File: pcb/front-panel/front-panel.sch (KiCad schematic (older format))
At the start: 26 parts, among them J1 HEADER-1x05, J2 HEADER-1x01, J3 HEADER-1x01, J4 HEADER-1x01, J5 HEADER-1x01, U1 ER-OLED1602-4W, U2 LT1109CS8-12

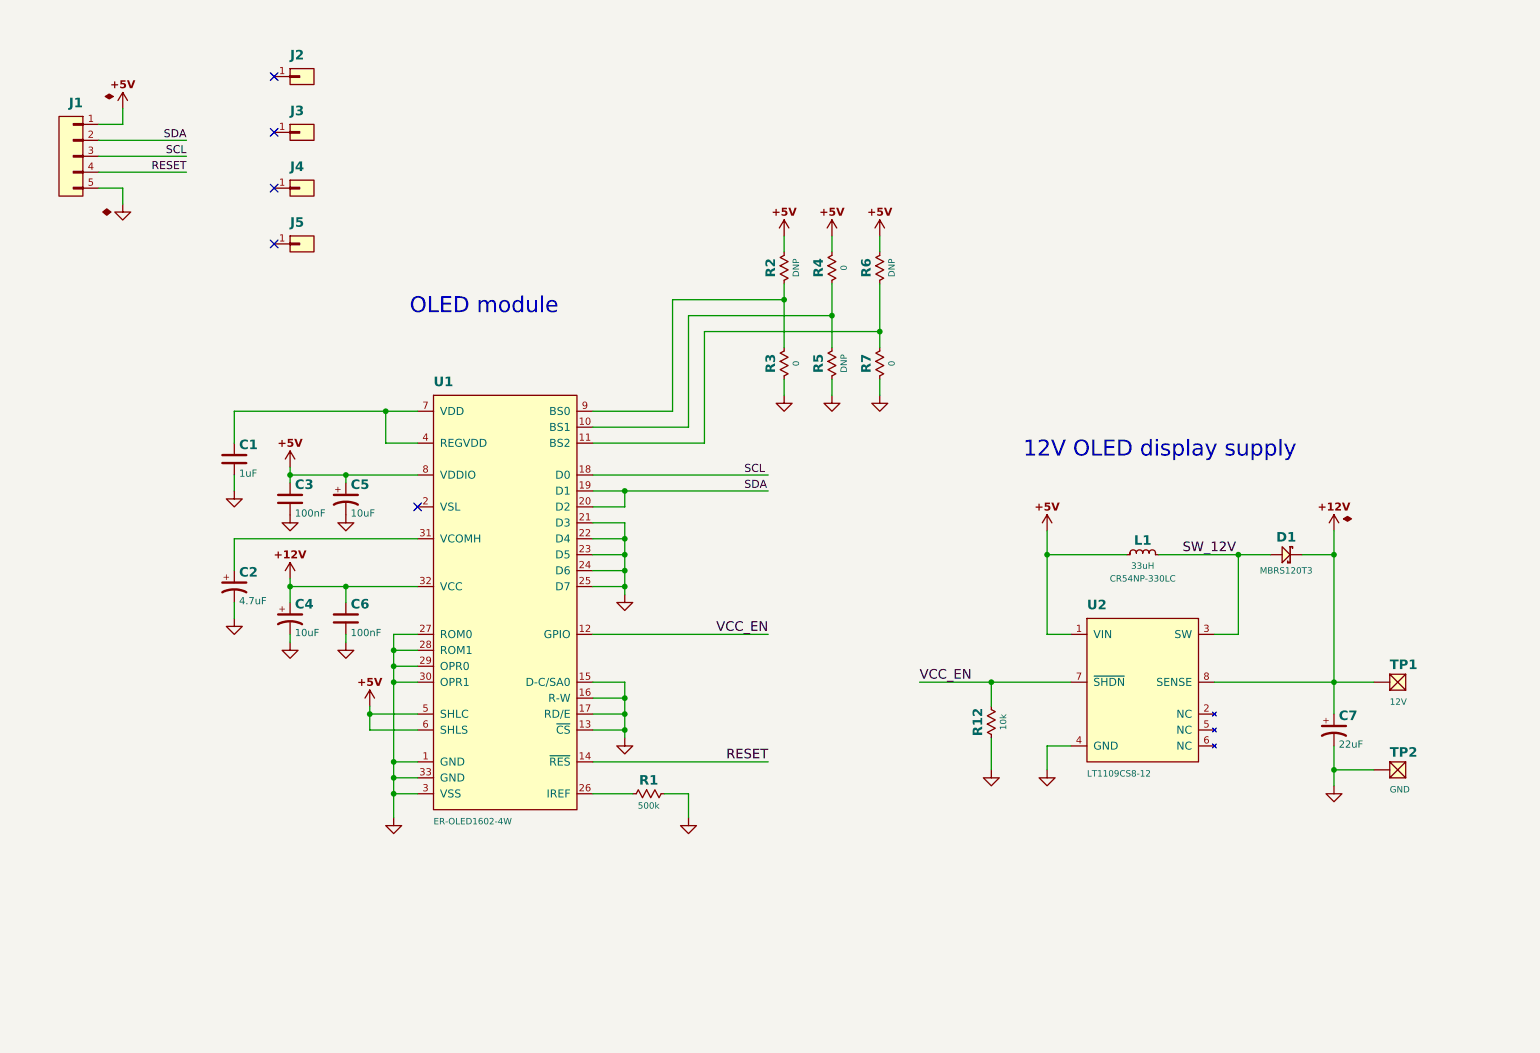
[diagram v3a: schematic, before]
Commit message: EN of 12V suply controlled from MCU instead of LCD GPIO
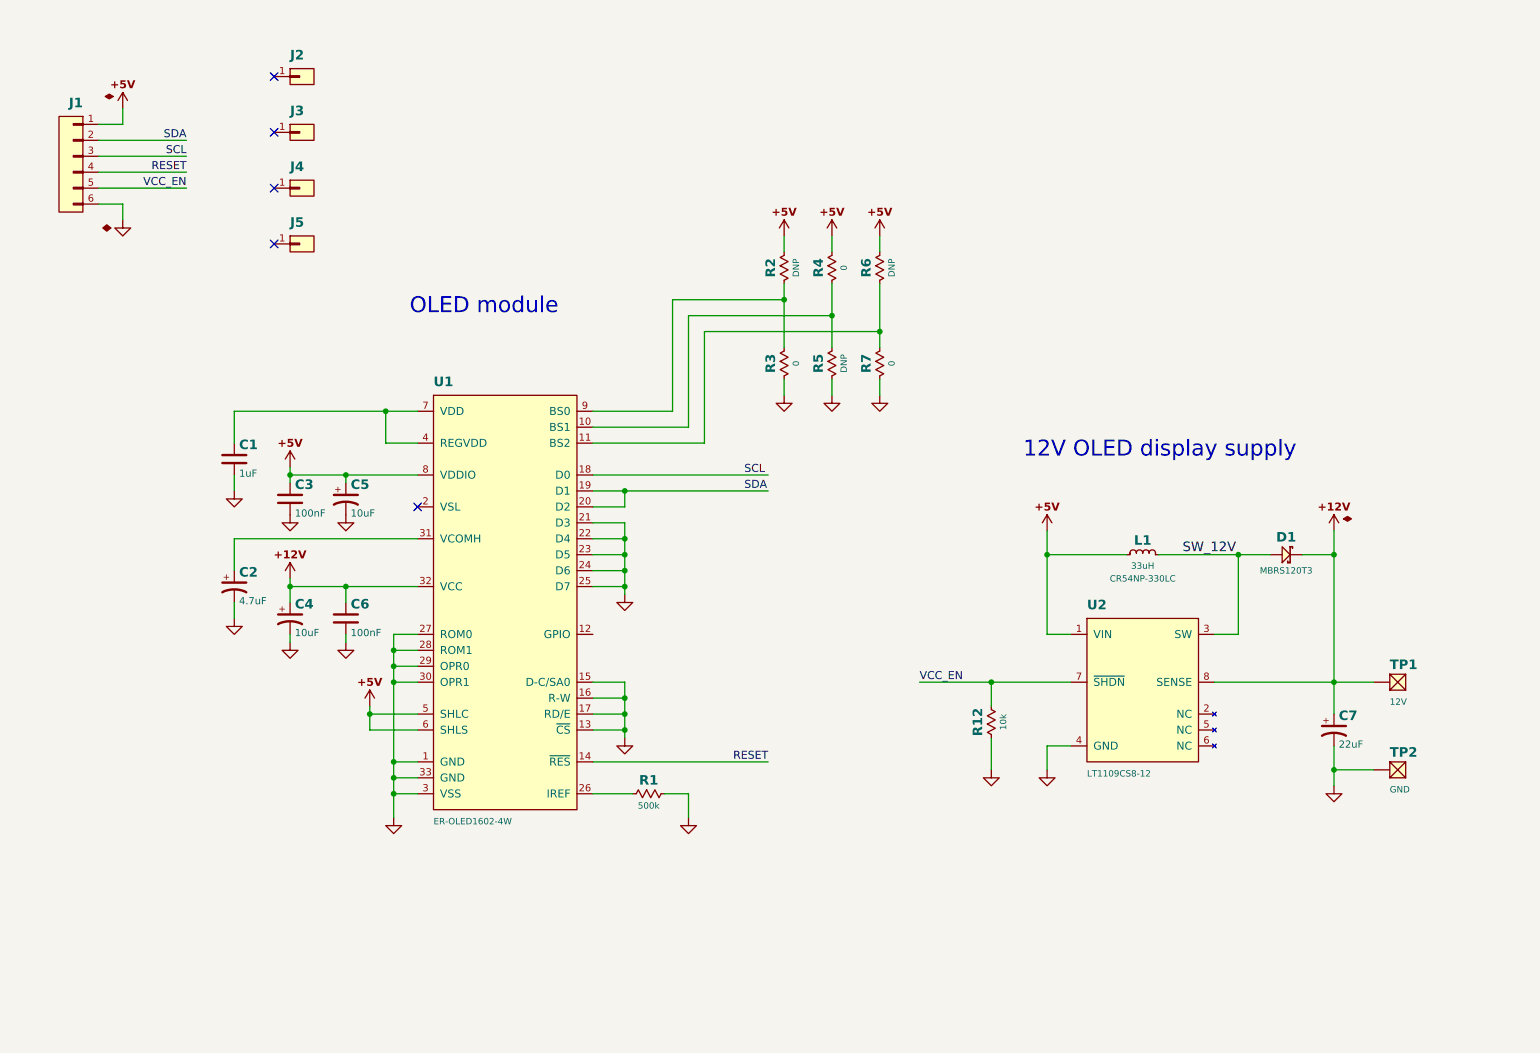
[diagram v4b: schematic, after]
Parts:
- removed J1: HEADER-1x05, Conn-Wire-Pads:WP-50mil-1x05, symbol HEADER-1x05
- added J1: HEADER-1x06, Conn-Wire-Pads:WP-50mil-1x06, symbol HEADER-1x06
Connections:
- net +5V: now also J1.1 (P1)
- net GND: now also J1.6 (P6)
- net RESET: now also J1.4 (P4)
- net SCL: now also J1.3 (P3)
- net SDA: now also J1.2 (P2)
- net VCC_EN: now also J1.5 (P5); no longer U1.12 (GPIO)
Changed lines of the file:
@@
 $EndComp
 $Comp
-L GND #PWR01
+L GND #PWR12
 U 1 1 562D385F
 P 3350 5800
-F 0 "#PWR01" H 3350 5850 30  0001 C CNN
+F 0 "#PWR12" H 3350 5850 30  0001 C CNN
 F 1 "GND" H 3350 5675 30  0001 C CNN
 F 2 "" H 3350 5800 60  0000 C CNN
@@
 $EndComp
 $Comp
-L GND #PWR02
+L GND #PWR15
 U 1 1 562D3A86
 P 5200 5800
-F 0 "#PWR02" H 5200 5850 30  0001 C CNN
+F 0 "#PWR15" H 5200 5850 30  0001 C CNN
 F 1 "GND" H 5200 5675 30  0001 C CNN
 F 2 "" H 5200 5800 60  0000 C CNN
@@
 $EndComp
 $Comp
-L GND #PWR03
+L GND #PWR13
 U 1 1 562D3B1B
 P 4800 4400
-F 0 "#PWR03" H 4800 4450 30  0001 C CNN
+F 0 "#PWR13" H 4800 4450 30  0001 C CNN
 F 1 "GND" H 4800 4275 30  0001 C CNN
 F 2 "" H 4800 4400 60  0000 C CNN
@@
 $EndComp
 $Comp
-L GND #PWR04
+L GND #PWR14
 U 1 1 562D3DB7
 P 4800 5300
-F 0 "#PWR04" H 4800 5350 30  0001 C CNN
+F 0 "#PWR14" H 4800 5350 30  0001 C CNN
 F 1 "GND" H 4800 5175 30  0001 C CNN
 F 2 "" H 4800 5300 60  0000 C CNN
@@
 RESET
 $Comp
-L +5V #PWR05
+L +5V #PWR11
 U 1 1 577BF2B2
 P 3200 5100
-F 0 "#PWR05" H 3200 5325 30  0001 C CNN
+F 0 "#PWR11" H 3200 5325 30  0001 C CNN
 F 1 "+5V" V 3125 5100 30  0001 C CNN
 F 2 "" H 3200 5100 60  0000 C CNN
@@
 $EndComp
 $Comp
-L GND #PWR06
+L GND #PWR8
 U 1 1 577BF2C9
 P 2700 4700
-F 0 "#PWR06" H 2700 4750 30  0001 C CNN
+F 0 "#PWR8" H 2700 4750 30  0001 C CNN
 F 1 "GND" H 2700 4575 30  0001 C CNN
 F 2 "" H 2700 4700 60  0000 C CNN
@@
 $EndComp
 $Comp
-L GND #PWR07
+L GND #PWR4
 U 1 1 577BF40D
 P 2350 4550
-F 0 "#PWR07" H 2350 4600 30  0001 C CNN
+F 0 "#PWR4" H 2350 4600 30  0001 C CNN
 F 1 "GND" H 2350 4425 30  0001 C CNN
 F 2 "" H 2350 4550 60  0000 C CNN
@@
 $EndComp
 $Comp
-L GND #PWR08
+L GND #PWR6
 U 1 1 577BF783
 P 2700 3900
-F 0 "#PWR08" H 2700 3950 30  0001 C CNN
+F 0 "#PWR6" H 2700 3950 30  0001 C CNN
 F 1 "GND" H 2700 3775 30  0001 C CNN
 F 2 "" H 2700 3900 60  0000 C CNN
@@
 $EndComp
 $Comp
-L +12V #PWR09
+L +12V #PWR7
 U 1 1 577BF7EA
 P 2700 4300
-F 0 "#PWR09" H 2700 4525 30  0001 C CNN
+F 0 "#PWR7" H 2700 4525 30  0001 C CNN
 F 1 "+12V" V 2625 4300 30  0001 C CNN
 F 2 "" H 2700 4300 60  0000 C CNN
@@
 $EndComp
 $Comp
-L GND #PWR010
+L GND #PWR9
 U 1 1 577C0C15
 P 3050 3900
-F 0 "#PWR010" H 3050 3950 30  0001 C CNN
+F 0 "#PWR9" H 3050 3950 30  0001 C CNN
 F 1 "GND" H 3050 3775 30  0001 C CNN
 F 2 "" H 3050 3900 60  0000 C CNN
@@
 $EndComp
 $Comp
-L GND #PWR011
+L GND #PWR10
 U 1 1 577C0F0C
 P 3050 4700
-F 0 "#PWR011" H 3050 4750 30  0001 C CNN
+F 0 "#PWR10" H 3050 4750 30  0001 C CNN
 F 1 "GND" H 3050 4575 30  0001 C CNN
 F 2 "" H 3050 4700 60  0000 C CNN
@@
 $EndComp
 $Comp
-L GND #PWR012
+L GND #PWR3
 U 1 1 577C147B
 P 2350 3750
-F 0 "#PWR012" H 2350 3800 30  0001 C CNN
+F 0 "#PWR3" H 2350 3800 30  0001 C CNN
 F 1 "GND" H 2350 3625 30  0001 C CNN
 F 2 "" H 2350 3750 60  0000 C CNN
@@
 $EndComp
 $Comp
-L +5V #PWR013
+L +5V #PWR5
 U 1 1 577C33A0
 P 2700 3600
-F 0 "#PWR013" H 2700 3825 30  0001 C CNN
+F 0 "#PWR5" H 2700 3825 30  0001 C CNN
 F 1 "+5V" V 2625 3600 30  0001 C CNN
 F 2 "" H 2700 3600 60  0000 C CNN
@@
 	1    0    0    -1
 $EndComp
-Text Label 5700 5450 2    60   ~ 0
+Text Label 5700 5450 2    50   ~ 0
 RESET
 $Comp
@@
 $EndComp
 $Comp
-L +5V #PWR014
+L +5V #PWR20
 U 1 1 577C7501
 P 6400 2150
-F 0 "#PWR014" H 6400 2375 30  0001 C CNN
+F 0 "#PWR20" H 6400 2375 30  0001 C CNN
 F 1 "+5V" V 6325 2150 30  0001 C CNN
 F 2 "" H 6400 2150 60  0000 C CNN
@@
 $EndComp
 $Comp
-L +5V #PWR015
+L +5V #PWR18
 U 1 1 577C7549
 P 6100 2150
-F 0 "#PWR015" H 6100 2375 30  0001 C CNN
+F 0 "#PWR18" H 6100 2375 30  0001 C CNN
 F 1 "+5V" V 6025 2150 30  0001 C CNN
 F 2 "" H 6100 2150 60  0000 C CNN
@@
 $EndComp
 $Comp
-L +5V #PWR016
+L +5V #PWR16
 U 1 1 577C759C
 P 5800 2150
-F 0 "#PWR016" H 5800 2375 30  0001 C CNN
+F 0 "#PWR16" H 5800 2375 30  0001 C CNN
 F 1 "+5V" V 5725 2150 30  0001 C CNN
 F 2 "" H 5800 2150 60  0000 C CNN
@@
 $EndComp
 $Comp
-L GND #PWR017
+L GND #PWR17
 U 1 1 577C77E7
 P 5800 3150
-F 0 "#PWR017" H 5800 3200 30  0001 C CNN
+F 0 "#PWR17" H 5800 3200 30  0001 C CNN
 F 1 "GND" H 5800 3025 30  0001 C CNN
 F 2 "" H 5800 3150 60  0000 C CNN
@@
 $EndComp
 $Comp
-L GND #PWR018
+L GND #PWR19
 U 1 1 577C7828
 P 6100 3150
-F 0 "#PWR018" H 6100 3200 30  0001 C CNN
+F 0 "#PWR19" H 6100 3200 30  0001 C CNN
 F 1 "GND" H 6100 3025 30  0001 C CNN
 F 2 "" H 6100 3150 60  0000 C CNN
@@
 $EndComp
 $Comp
-L GND #PWR019
+L GND #PWR21
 U 1 1 577C7869
 P 6400 3150
-F 0 "#PWR019" H 6400 3200 30  0001 C CNN
+F 0 "#PWR21" H 6400 3200 30  0001 C CNN
 F 1 "GND" H 6400 3025 30  0001 C CNN
 F 2 "" H 6400 3150 60  0000 C CNN
@@
 	1    0    0    -1
 $EndComp
-Text Label 5700 4650 2    60   ~ 0
-VCC_EN
-$Comp
-L +5V #PWR020
+$Comp
+L +5V #PWR23
 U 1 1 5780AC08
 P 7450 4000
-F 0 "#PWR020" H 7450 4225 30  0001 C CNN
+F 0 "#PWR23" H 7450 4225 30  0001 C CNN
 F 1 "+5V" V 7375 4000 30  0001 C CNN
 F 2 "" H 7450 4000 60  0000 C CNN
@@
 $EndComp
 $Comp
-L GND #PWR021
+L GND #PWR24
 U 1 1 5780CB67
 P 7450 5500
-F 0 "#PWR021" H 7450 5550 30  0001 C CNN
+F 0 "#PWR24" H 7450 5550 30  0001 C CNN
 F 1 "GND" H 7450 5375 30  0001 C CNN
 F 2 "" H 7450 5500 60  0000 C CNN
@@
 $EndComp
 $Comp
-L SUP_+12V #PWR022
+L SUP_+12V #PWR25
 U 1 1 5780D7CE
 P 9250 4000
-F 0 "#PWR022" H 9250 4225 30  0001 C CNN
+F 0 "#PWR25" H 9250 4225 30  0001 C CNN
 F 1 "SUP_+12V" V 9175 4000 30  0001 C CNN
 F 2 "" H 9150 4125 60  0001 C CNN
@@
 	1    0    0    -1
 $EndComp
-Text Label 6650 4950 0    60   ~ 0
+Text Label 6650 4950 0    50   ~ 0
 VCC_EN
 $Comp
@@
 $EndComp
 $Comp
-L GND #PWR023
+L GND #PWR26
 U 1 1 57810AEC
 P 9250 5600
-F 0 "#PWR023" H 9250 5650 30  0001 C CNN
+F 0 "#PWR26" H 9250 5650 30  0001 C CNN
 F 1 "GND" H 9250 5475 30  0001 C CNN
 F 2 "" H 9250 5600 60  0000 C CNN
@@
 $EndComp
 $Comp
-L SUP_GND #PWR024
+L SUP_GND #PWR2
 U 1 1 5781A10F
-P 1650 1950
-F 0 "#PWR024" H 1650 2000 30  0001 C CNN
-F 1 "SUP_GND" H 1650 1825 30  0001 C CNN
-F 2 "" H 1650 1950 60  0000 C CNN
-F 3 "" H 1650 1950 60  0000 C CNN
-	1    1650 1950
+P 1650 2050
+F 0 "#PWR2" H 1650 2100 30  0001 C CNN
+F 1 "SUP_GND" H 1650 1925 30  0001 C CNN
+F 2 "" H 1650 2050 60  0000 C CNN
+F 3 "" H 1650 2050 60  0000 C CNN
+	1    1650 2050
 	-1   0    0    -1
 $EndComp
 $Comp
-L SUP_+5V #PWR025
+L SUP_+5V #PWR1
 U 1 1 5781A17B
 P 1650 1350
-F 0 "#PWR025" H 1650 1575 30  0001 C CNN
+F 0 "#PWR1" H 1650 1575 30  0001 C CNN
 F 1 "SUP_+5V" V 1575 1350 30  0001 C CNN
 F 2 "" H 1550 1475 60  0001 C CNN
 F 3 "" H 1650 1575 60  0001 C CNN
 	1    1650 1350
-	-1   0    0    -1
-$EndComp
-$Comp
-L HEADER-1x05 J1
-U 1 1 563069BD
-P 1350 1650
-F 0 "J1" H 1300 1950 60  0000 L BNB
-F 1 "HEADER-1x05" V 1500 1650 40  0001 C CNN
-F 2 "Conn-Wire-Pads:WP-50mil-1x05" H 1350 1650 60  0001 C CNN
-F 3 "" H 1350 1650 60  0001 C CNN
-F 4 "-" H 1300 2050 40  0001 L BNN "Part"
-F 5 "Virtual" H 1300 2150 40  0001 L BNN "Family"
-	1    1350 1650
 	-1   0    0    -1
 $EndComp
@@
 $EndComp
 $Comp
-L GND #PWR026
+L GND #PWR22
 U 1 1 5782CD1E
 P 7100 5500
-F 0 "#PWR026" H 7100 5550 30  0001 C CNN
+F 0 "#PWR22" H 7100 5550 30  0001 C CNN
 F 1 "GND" H 7100 5375 30  0001 C CNN
 F 2 "" H 7100 5500 60  0000 C CNN
@@
 Connection ~ 4800 5150
 Wire Wire Line
-	1500 1850 1650 1850
-Wire Wire Line
-	1650 1850 1650 1950
+	1500 1950 1650 1950
+Wire Wire Line
+	1650 1950 1650 2050
 Wire Wire Line
 	1500 1450 1650 1450
@@
 Wire Wire Line
 	6400 2150 6400 2250
-Wire Wire Line
-	4600 4650 5700 4650
 Wire Wire Line
 	8500 4650 8650 4650
@@
 	1    0    0    -1
 $EndComp
+$Comp
+L HEADER-1x06 J1
+U 1 1 578A678A
+P 1350 1700
+F 0 "J1" H 1300 2050 60  0000 L BNB
+F 1 "HEADER-1x06" V 1500 1700 40  0001 C CNN
+F 2 "Conn-Wire-Pads:WP-50mil-1x06" H 1350 1700 60  0001 C CNN
+F 3 "" H 1350 1700 60  0001 C CNN
+F 4 "-" H 1300 2150 40  0001 L BNN "Part"
+F 5 "Virtual" H 1300 2250 40  0001 L BNN "Family"
+	1    1350 1700
+	-1   0    0    -1
+$EndComp
+Wire Wire Line
+	1500 1850 2050 1850
+Text Label 2050 1850 2    50   ~ 0
+VCC_EN
 $EndSCHEMATC
